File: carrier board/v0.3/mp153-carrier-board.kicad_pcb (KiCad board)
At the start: 2 copper layers, 87.2 x 87.4 mm, 99 parts, among them J1 USB-C_Receptacle_Molex_217179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, J10 3.5mm_Mono_Switched_sm, J11 3.5mm_Mono_Switched_sm, J12 3.5mm_Mono_Switched_sm, J13 3.5mm_Mono_Switched_sm, J2 Eurorack_Power_10pin_Shrouded, J5 3.5mm_Mono_Switched_sm, J9 3.5mm_Mono_Switched_sm, U1 TL072H, U11 TL072H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

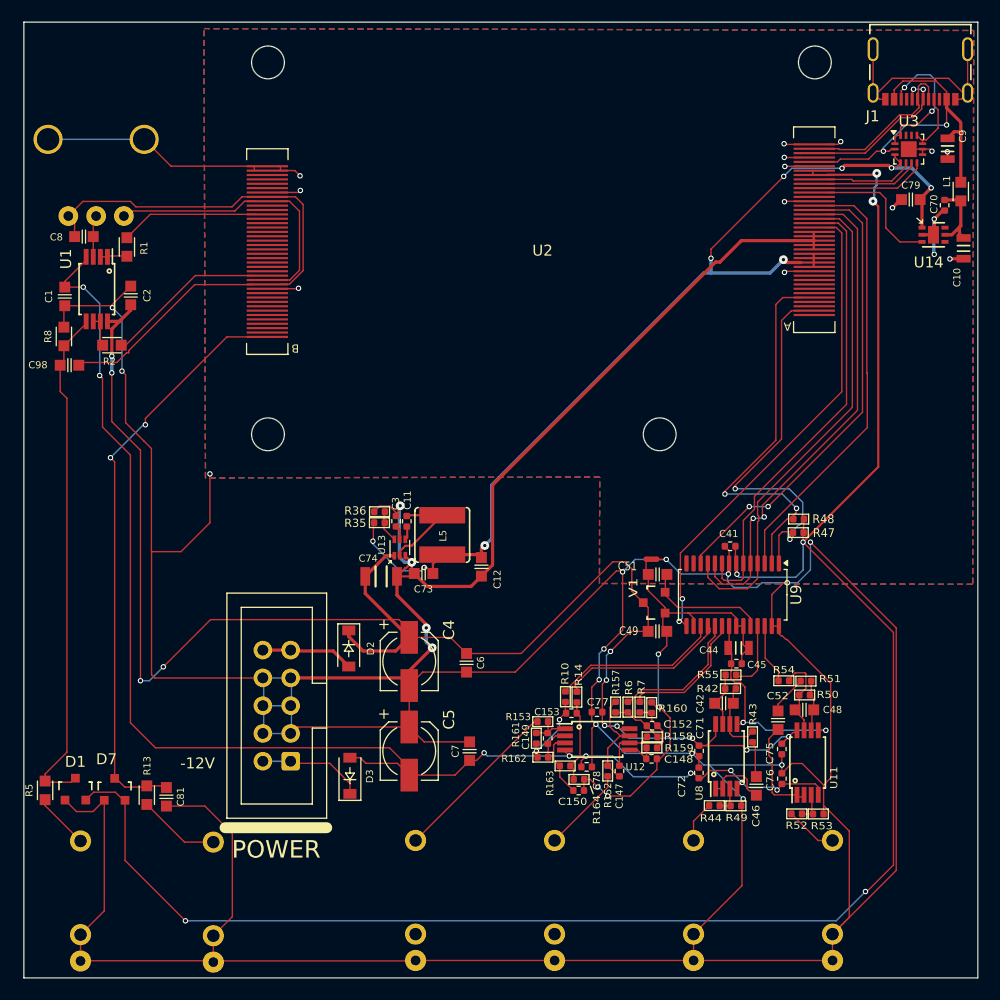
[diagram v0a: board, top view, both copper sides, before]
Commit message: carrier board v0.3: finish schematic and PCB
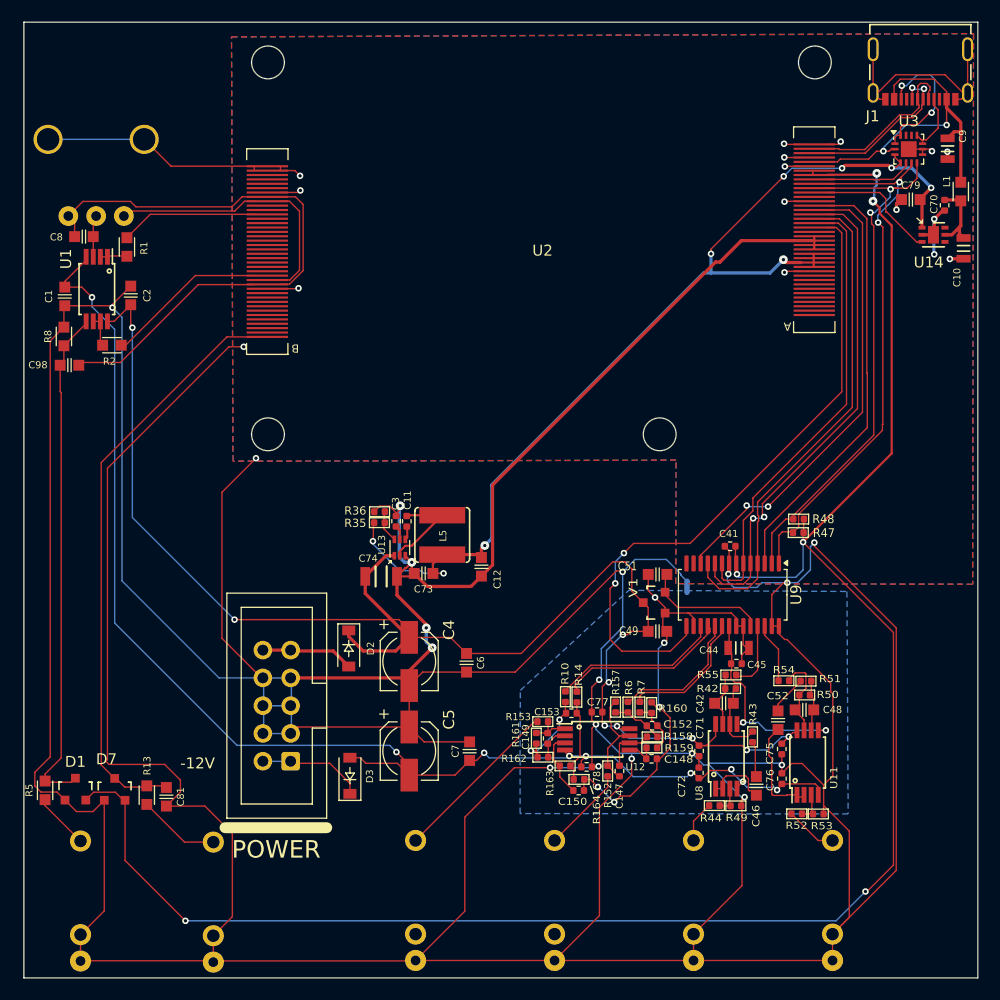
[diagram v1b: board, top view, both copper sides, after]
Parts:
- removed Devboard-stand-in: mp153-dev-board-p1, 4ms_Symbol:4msLogo_3.8x1.7mm
- NT1: moved to B.Cu
- moved NT1 4.11 mm to (225.4, 126.8), turned to 90 degrees
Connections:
- R47 pad 1: /I2C3_SCL -> /I2C6_SCL
- R48 pad 1: /I2C3_SDA -> /I2C6_SDA
- U2 pad A3: /I2C6_SCL -> unconnected-(U2-PA8-PadA3)
- U2 pad A9: /I2C6_SDA -> unconnected-(U2-PC9-PadA9)
- U2 pad B26: VREF+ -> GNDADC
- U2 pad B28: GNDADC -> VREF+
- U9 pad 1: /I2C3_SCL -> /I2C6_SCL
- U9 pad 2: /I2C3_SDA -> /I2C6_SDA
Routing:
- net GND: track 576.2 -> 733.4 mm, vias 33 -> 34
- net (no net): track 70.1 -> 0.00 mm, vias 4 -> 0
- net /I2C6_SCL: track 8.68 -> 49.8 mm, vias 0 -> 2
- net /I2C6_SDA: track 9.46 -> 50.3 mm, vias 0 -> 2
- net /CODEC_RESET: track 44.2 -> 59.4 mm
- net +12V: track 150.6 -> 138.3 mm, vias 11 -> 9
- net -12V: track 124.5 -> 120.6 mm
- net +5V: track 92.1 -> 93.8 mm
- net Net-(C153-Pad1): track 6.90 -> 7.93 mm
- net +3V3: track 173.3 -> 174.3 mm
- net GNDA: track 44.9 -> 43.9 mm, vias 4 -> 5
- net /USB_5V_ENABLE: track 12.1 -> 11.2 mm
- net /GATE1_IN: track 53.0 -> 53.6 mm, vias 2 -> 0
- added copper zone on B.Cu, net GNDA
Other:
- board text added: "AUDIO IN L"
- board text added: "AUDIO IN R"
- board text added: "AUDIO OUT L"
- board text added: "AUDIO OUT R"
- board text added: "CV IN"
- board text added: "GATE IN"

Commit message: JLC Producton files for carrier board v0.3
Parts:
- removed U2: ~, mp153-devboard:mp153-devboard-v0.1-sockets
- added ?: , , F.Cu at (222.9, 112.8)
- added ?: , , F.Cu at (187.1, 112.8)
- added ?: , , F.Cu at (237.1, 78.8)
- added ?: , , F.Cu at (187.1, 78.8)
- added J3: Socket_02x40_P0.4mm_W3.0mm_SMT, mp153-devboard:Connector-80socket-P0.4mm-W3.0mm, F.Cu at (237.1, 94.1)
- added J4: Socket_02x40_P0.4mm_W3.0mm_SMT, mp153-devboard:Connector-80socket-P0.4mm-W3.0mm, F.Cu at (187.1, 96.1)
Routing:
- net GND: track 733.4 -> 755.4 mm, vias 34 -> 33
- net +5V: track 93.8 -> 103.4 mm
- net VREF+: track 22.1 -> 26.9 mm
- net GNDADC: track 50.6 -> 55.4 mm
- net +3V3: track 174.3 -> 179.1 mm
- net /USB_5V_ENABLE: track 11.2 -> 13.6 mm
- net /SAI_SD_B: track 39.5 -> 41.9 mm
- net /SAI_SD_A: track 42.2 -> 44.6 mm
- net /SAI_SCK: track 44.9 -> 47.3 mm
- net /SAI_MCLK: track 41.1 -> 43.5 mm
- net /SAI_FS: track 44.8 -> 47.2 mm
- net /I2C6_SDA: track 50.3 -> 52.7 mm
- net /I2C6_SCL: track 49.8 -> 52.1 mm
- net /CODEC_RESET: track 59.4 -> 61.7 mm
- net /USB_VBUS_JACK: track 33.0 -> 35.4 mm
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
